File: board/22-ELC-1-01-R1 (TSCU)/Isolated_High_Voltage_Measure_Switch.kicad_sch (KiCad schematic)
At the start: 18 parts, among them U10 RFMM-0505S, U13 ACPL-C79B, U14 LM358

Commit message: Ready for review
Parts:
- renumbered C19 to C25, C35 to C26, C21 to C27, C22 to C28, C25 to C29, C26 to C30, R31 to R43, R32 to R44, R33 to R45, R34 to R46, R35 to R47, R37 to R48, R39 to R49, R38 to R50, R41 to R51, U13 to U10, U14 to U11, U10 to U9

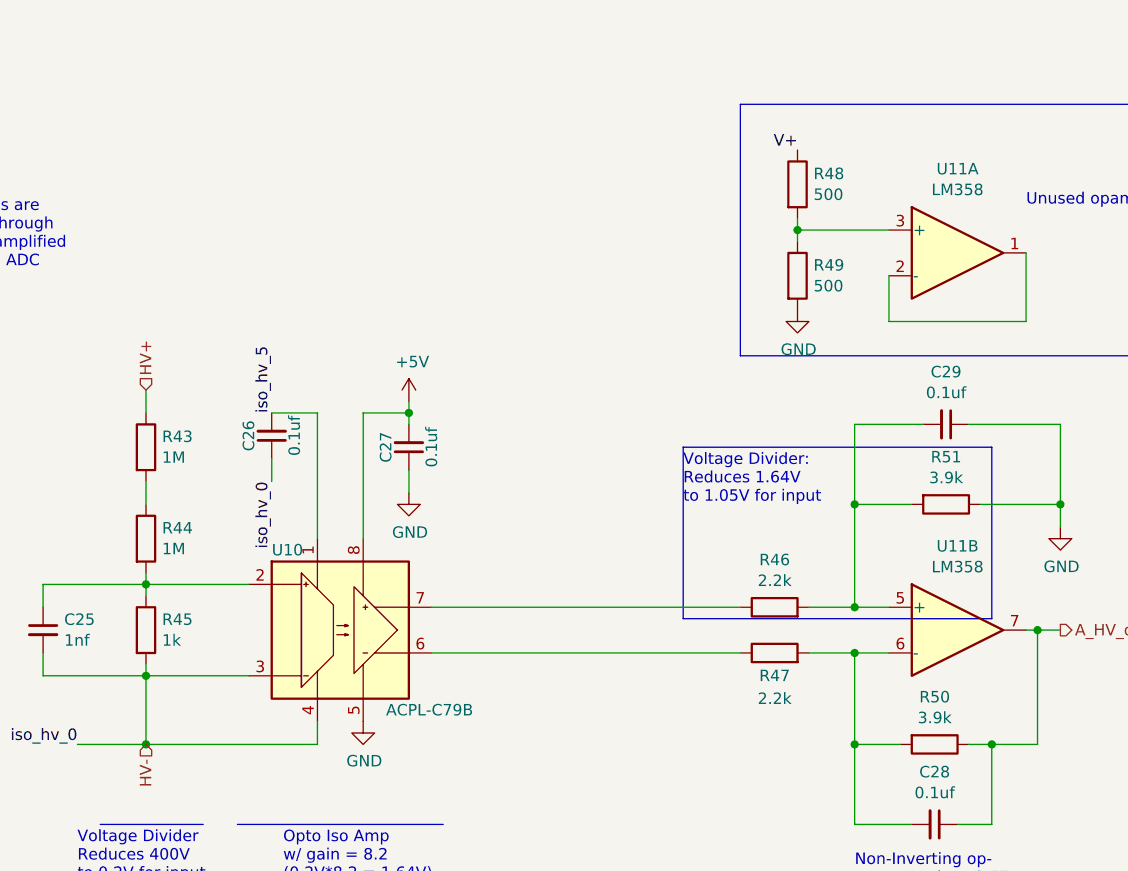
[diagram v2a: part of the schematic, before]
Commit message: All good except need to switch everything to accepting 24v power
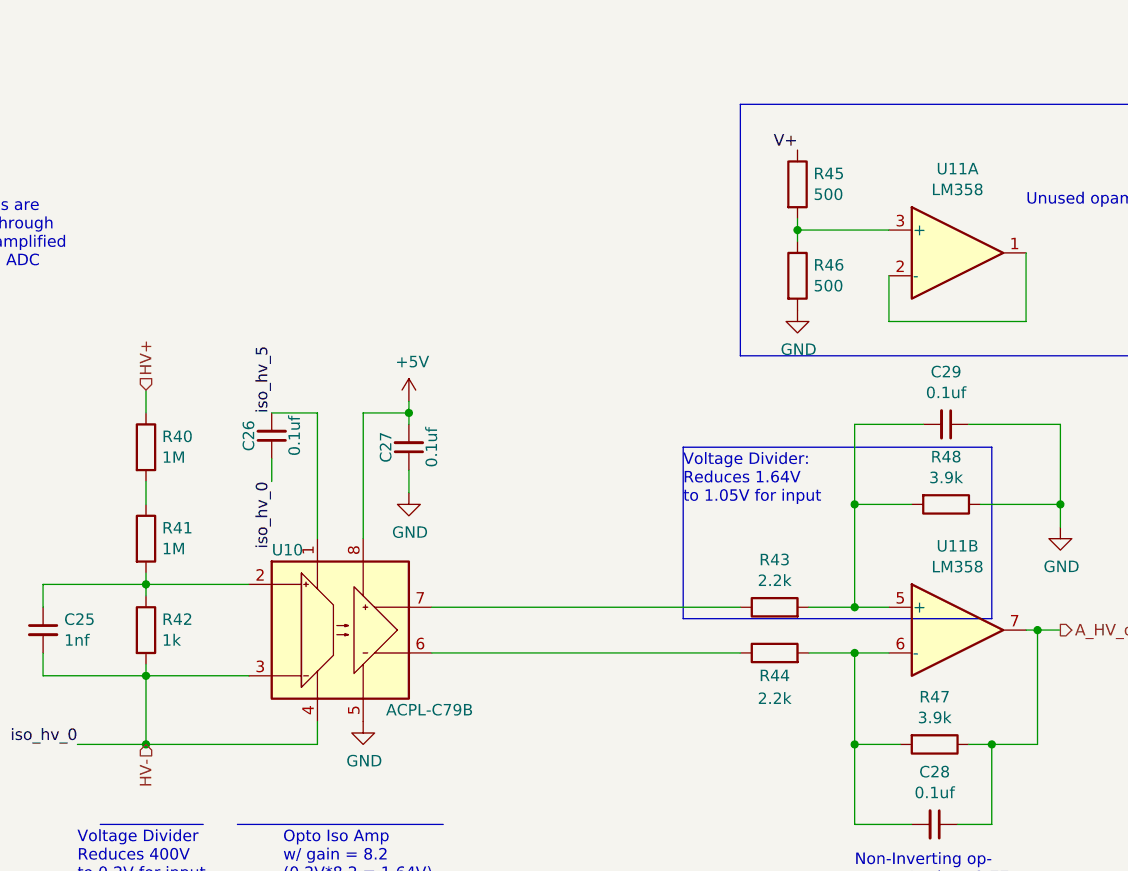
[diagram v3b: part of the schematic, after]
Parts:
- R45: renamed from R48; footprint (none) -> Resistor_SMD:R_0603_1608Metric_Pad0.98x0.95mm_HandSolder
- R46: renamed from R49; footprint (none) -> Resistor_SMD:R_0603_1608Metric_Pad0.98x0.95mm_HandSolder
- renumbered R43 to R40, R44 to R41, R45 to R42, R46 to R43, R47 to R44, R50 to R47, R51 to R48
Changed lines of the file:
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@@
   (symbol (lib_id "Device:R") (at 146.05 134.62 0) (unit 1)
     (in_bom yes) (on_board yes)
-    (property "Reference" "R45" (id 0) (at 147.828 133.4516 0)
+    (property "Reference" "R42" (id 0) (at 147.828 133.4516 0)
       (effects (font (size 1.27 1.27)) (justify left))
     )
@@
   (symbol (lib_id "Device:R") (at 146.05 124.46 0) (unit 1)
     (in_bom yes) (on_board yes)
-    (property "Reference" "R44" (id 0) (at 147.828 123.2916 0)
+    (property "Reference" "R41" (id 0) (at 147.828 123.2916 0)
       (effects (font (size 1.27 1.27)) (justify left))
     )
@@
   (symbol (lib_id "Device:R") (at 146.05 114.3 0) (unit 1)
     (in_bom yes) (on_board yes)
-    (property "Reference" "R43" (id 0) (at 147.828 113.1316 0)
+    (property "Reference" "R40" (id 0) (at 147.828 113.1316 0)
       (effects (font (size 1.27 1.27)) (justify left))
     )
@@
   (symbol (lib_id "Device:R") (at 215.9 132.08 90) (unit 1)
     (in_bom yes) (on_board yes)
-    (property "Reference" "R46" (id 0) (at 215.9 126.8222 90))
+    (property "Reference" "R43" (id 0) (at 215.9 126.8222 90))
     (property "Value" "2.2k" (id 1) (at 215.9 129.1336 90))
     (property "Footprint" "Resistor_SMD:R_0603_1608Metric_Pad0.98x0.95mm_HandSolder" (id 2) (at 215.9 133.858 90)
@@
   (symbol (lib_id "Device:R") (at 215.9 137.16 90) (unit 1)
     (in_bom yes) (on_board yes)
-    (property "Reference" "R47" (id 0) (at 215.9 139.7 90))
+    (property "Reference" "R44" (id 0) (at 215.9 139.7 90))
     (property "Value" "2.2k" (id 1) (at 215.9 142.24 90))
     (property "Footprint" "Resistor_SMD:R_0603_1608Metric_Pad0.98x0.95mm_HandSolder" (id 2) (at 215.9 138.938 90)
@@
   (symbol (lib_id "Device:R") (at 234.95 120.65 270) (unit 1)
     (in_bom yes) (on_board yes)
-    (property "Reference" "R51" (id 0) (at 234.95 115.3922 90))
+    (property "Reference" "R48" (id 0) (at 234.95 115.3922 90))
     (property "Value" "3.9k" (id 1) (at 234.95 117.7036 90))
     (property "Footprint" "Resistor_SMD:R_0603_1608Metric_Pad0.98x0.95mm_HandSolder" (id 2) (at 234.95 118.872 90)
@@
   (symbol (lib_id "Device:R") (at 233.68 147.32 270) (unit 1)
     (in_bom yes) (on_board yes)
-    (property "Reference" "R50" (id 0) (at 233.68 142.0622 90))
+    (property "Reference" "R47" (id 0) (at 233.68 142.0622 90))
     (property "Value" "3.9k" (id 1) (at 233.68 144.3736 90))
     (property "Footprint" "Resistor_SMD:R_0603_1608Metric_Pad0.98x0.95mm_HandSolder" (id 2) (at 233.68 145.542 90)
@@
   (symbol (lib_id "Device:R") (at 218.44 85.09 0) (unit 1)
     (in_bom yes) (on_board yes)
-    (property "Reference" "R48" (id 0) (at 220.218 83.9216 0)
+    (property "Reference" "R45" (id 0) (at 220.218 83.9216 0)
       (effects (font (size 1.27 1.27)) (justify left))
     )
@@
       (effects (font (size 1.27 1.27)) (justify left))
     )
-    (property "Footprint" "" (id 2) (at 216.662 85.09 90)
+    (property "Footprint" "Resistor_SMD:R_0603_1608Metric_Pad0.98x0.95mm_HandSolder" (id 2) (at 216.662 85.09 90)
       (effects (font (size 1.27 1.27)) hide)
     )
@@
   (symbol (lib_id "Device:R") (at 218.44 95.25 0) (unit 1)
     (in_bom yes) (on_board yes)
-    (property "Reference" "R49" (id 0) (at 220.218 94.0816 0)
+    (property "Reference" "R46" (id 0) (at 220.218 94.0816 0)
       (effects (font (size 1.27 1.27)) (justify left))
     )
@@
       (effects (font (size 1.27 1.27)) (justify left))
     )
-    (property "Footprint" "" (id 2) (at 216.662 95.25 90)
-      (effects (font (size 1.27 1.27)) hide)
-    )
+    (property "Footprint" "Resistor_SMD:R_0603_1608Metric_Pad0.98x0.95mm_HandSolder" (id 2) (at 216.662 95.25 90)
+      (effects (font (size 1.27 1.27)) hide)
+    )

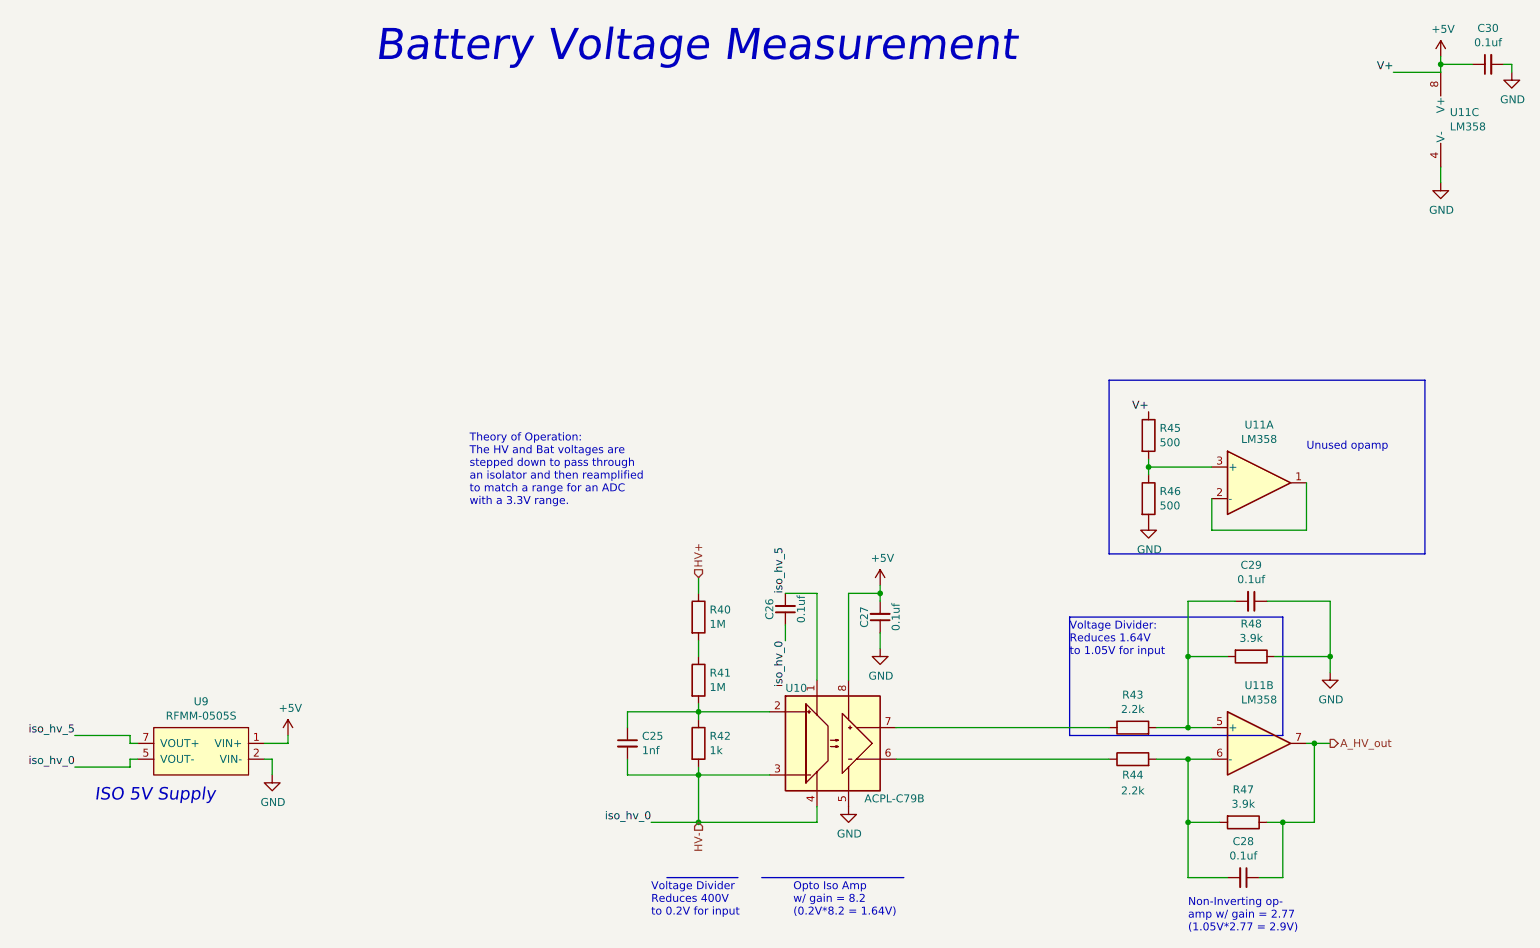
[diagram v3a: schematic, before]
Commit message: Finalized schematic, started board layout
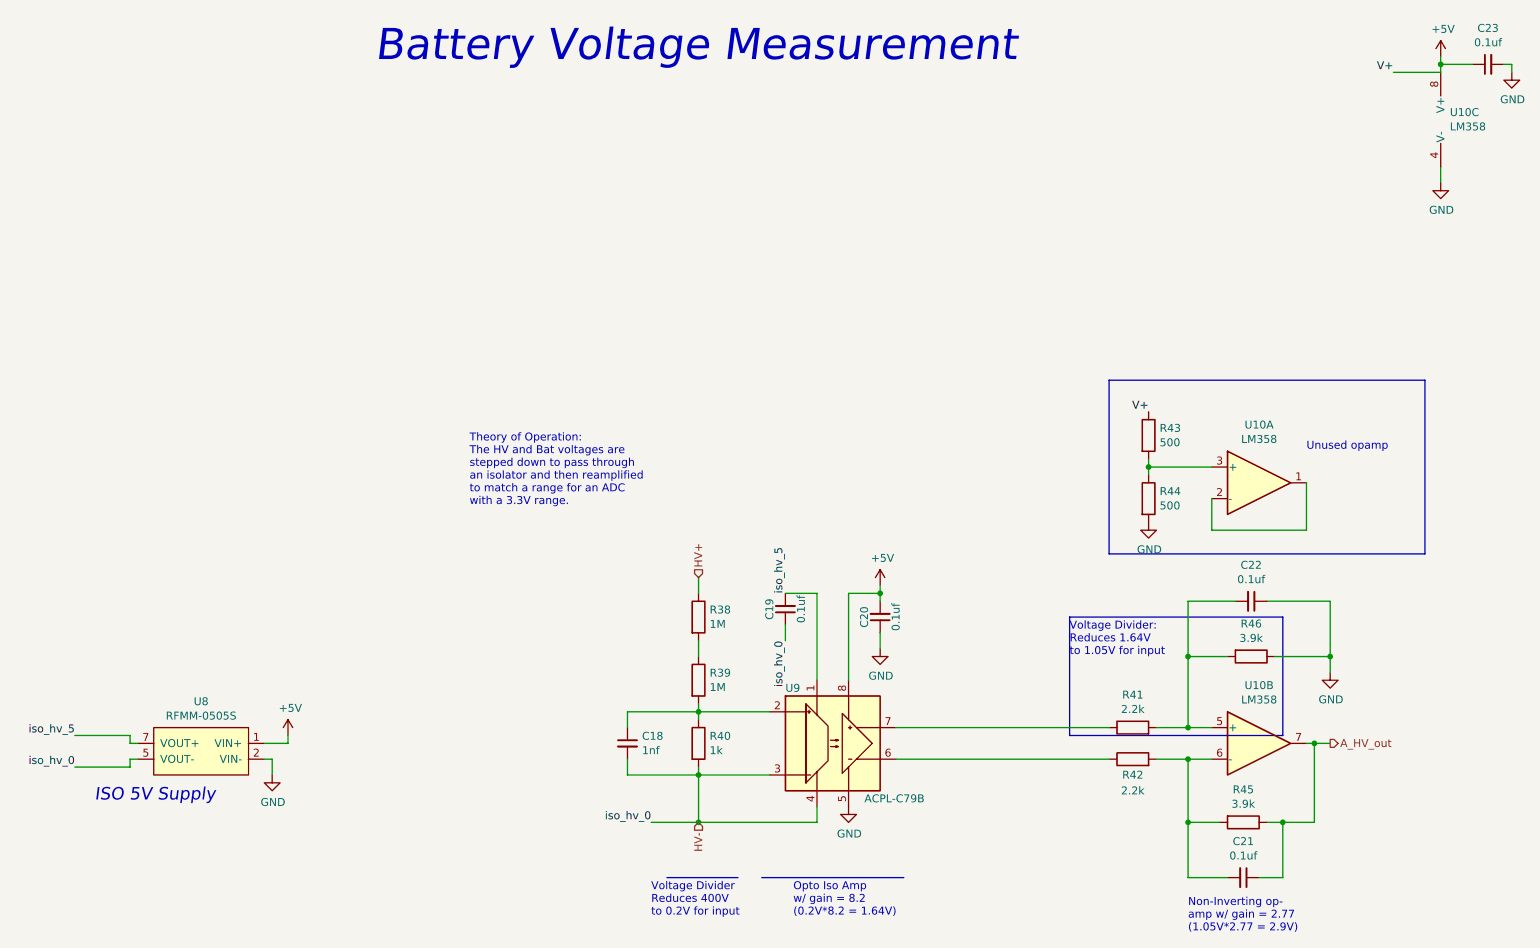
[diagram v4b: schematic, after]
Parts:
- C18: renamed from C25; footprint Capacitor_SMD:C_0603_1608Metric_Pad1.08x0.95mm_HandSolder -> Capacitor_SMD:C_0402_1005Metric
- C19: renamed from C26; footprint Capacitor_SMD:C_0603_1608Metric_Pad1.08x0.95mm_HandSolder -> Capacitor_SMD:C_0402_1005Metric
- C20: renamed from C27; footprint Capacitor_SMD:C_0603_1608Metric_Pad1.08x0.95mm_HandSolder -> Capacitor_SMD:C_0402_1005Metric
- C21: renamed from C28; footprint Capacitor_SMD:C_0603_1608Metric_Pad1.08x0.95mm_HandSolder -> Capacitor_SMD:C_0402_1005Metric
- C22: renamed from C29; footprint Capacitor_SMD:C_0603_1608Metric_Pad1.08x0.95mm_HandSolder -> Capacitor_SMD:C_0402_1005Metric
- C23: renamed from C30; footprint Capacitor_SMD:C_0603_1608Metric_Pad1.08x0.95mm_HandSolder -> Capacitor_SMD:C_0402_1005Metric
- R38: renamed from R40; footprint Resistor_SMD:R_1206_3216Metric_Pad1.30x1.75mm_HandSolder -> FixedTextSizes:R_0402_1005Metric
- R39: renamed from R41; footprint Resistor_SMD:R_1206_3216Metric_Pad1.30x1.75mm_HandSolder -> FixedTextSizes:R_0402_1005Metric
- R40: renamed from R42; footprint Resistor_SMD:R_0603_1608Metric_Pad0.98x0.95mm_HandSolder -> FixedTextSizes:R_0402_1005Metric
- R41: renamed from R43; footprint Resistor_SMD:R_0603_1608Metric_Pad0.98x0.95mm_HandSolder -> FixedTextSizes:R_0402_1005Metric
- R42: renamed from R44; footprint Resistor_SMD:R_0603_1608Metric_Pad0.98x0.95mm_HandSolder -> FixedTextSizes:R_0402_1005Metric
- R43: renamed from R45; footprint Resistor_SMD:R_0603_1608Metric_Pad0.98x0.95mm_HandSolder -> FixedTextSizes:R_0402_1005Metric
- R44: renamed from R46; footprint Resistor_SMD:R_0603_1608Metric_Pad0.98x0.95mm_HandSolder -> FixedTextSizes:R_0402_1005Metric
- R45: renamed from R47; footprint Resistor_SMD:R_0603_1608Metric_Pad0.98x0.95mm_HandSolder -> FixedTextSizes:R_0402_1005Metric
- R46: renamed from R48; footprint Resistor_SMD:R_0603_1608Metric_Pad0.98x0.95mm_HandSolder -> FixedTextSizes:R_0402_1005Metric
- renumbered U11 to U10, U9 to U8, U10 to U9

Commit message: More progress
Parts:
- C18, C19, C20, C21, C22, C23: footprint Capacitor_SMD:C_0402_1005Metric -> FixedTextSizes:C_0402_1005Metric_Pad0.74x0.62mm_HandSolder_Reasonable_Text_Size
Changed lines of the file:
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@@
   (symbol (lib_id "power:+5V") (at 80.01 133.35 0) (unit 1)
     (in_bom yes) (on_board yes)
-    (property "Reference" "#PWR082" (id 0) (at 80.01 137.16 0)
+    (property "Reference" "#PWR085" (id 0) (at 80.01 137.16 0)
       (effects (font (size 1.27 1.27)) hide)
     )
@@
   (symbol (lib_id "power:GND") (at 77.47 139.7 0) (unit 1)
     (in_bom yes) (on_board yes)
-    (property "Reference" "#PWR081" (id 0) (at 77.47 146.05 0)
+    (property "Reference" "#PWR084" (id 0) (at 77.47 146.05 0)
       (effects (font (size 1.27 1.27)) hide)
     )
@@
   (symbol (lib_id "power:GND") (at 265.43 44.45 0) (unit 1)
     (in_bom yes) (on_board yes)
-    (property "Reference" "#PWR089" (id 0) (at 265.43 50.8 0)
+    (property "Reference" "#PWR092" (id 0) (at 265.43 50.8 0)
       (effects (font (size 1.27 1.27)) hide)
     )
@@
     (property "Reference" "C23" (id 0) (at 273.05 19.5834 90))
     (property "Value" "0.1uf" (id 1) (at 273.05 21.8948 90))
-    (property "Footprint" "Capacitor_SMD:C_0402_1005Metric" (id 2) (at 273.05 25.4 0)
+    (property "Footprint" "FixedTextSizes:C_0402_1005Metric_Pad0.74x0.62mm_HandSolder_Reasonable_Text_Size" (id 2) (at 273.05 25.4 0)
       (effects (font (size 1.27 1.27)) hide)
     )
@@
   (symbol (lib_id "power:GND") (at 276.86 26.67 0) (unit 1)
     (in_bom yes) (on_board yes)
-    (property "Reference" "#PWR090" (id 0) (at 276.86 33.02 0)
+    (property "Reference" "#PWR093" (id 0) (at 276.86 33.02 0)
       (effects (font (size 1.27 1.27)) hide)
     )
@@
   (symbol (lib_id "power:GND") (at 170.18 144.78 0) (unit 1)
     (in_bom yes) (on_board yes)
-    (property "Reference" "#PWR083" (id 0) (at 170.18 151.13 0)
+    (property "Reference" "#PWR086" (id 0) (at 170.18 151.13 0)
       (effects (font (size 1.27 1.27)) hide)
     )
@@
   (symbol (lib_id "power:GND") (at 175.26 119.38 0) (unit 1)
     (in_bom yes) (on_board yes)
-    (property "Reference" "#PWR085" (id 0) (at 175.26 125.73 0)
+    (property "Reference" "#PWR088" (id 0) (at 175.26 125.73 0)
       (effects (font (size 1.27 1.27)) hide)
     )
@@
       (effects (font (size 1.27 1.27)) (justify left))
     )
-    (property "Footprint" "Capacitor_SMD:C_0402_1005Metric" (id 2) (at 134.62 134.62 0)
+    (property "Footprint" "FixedTextSizes:C_0402_1005Metric_Pad0.74x0.62mm_HandSolder_Reasonable_Text_Size" (id 2) (at 134.62 134.62 0)
       (effects (font (size 1.27 1.27)) hide)
     )
@@
     (property "Reference" "C20" (id 0) (at 172.72 114.3 90))
     (property "Value" "0.1uf" (id 1) (at 177.8 114.3 90))
-    (property "Footprint" "Capacitor_SMD:C_0402_1005Metric" (id 2) (at 175.26 114.3 0)
+    (property "Footprint" "FixedTextSizes:C_0402_1005Metric_Pad0.74x0.62mm_HandSolder_Reasonable_Text_Size" (id 2) (at 175.26 114.3 0)
       (effects (font (size 1.27 1.27)) hide)
     )
@@
     (property "Reference" "C21" (id 0) (at 233.68 150.3934 90))
     (property "Value" "0.1uf" (id 1) (at 233.68 152.7048 90))
-    (property "Footprint" "Capacitor_SMD:C_0402_1005Metric" (id 2) (at 233.68 156.21 0)
+    (property "Footprint" "FixedTextSizes:C_0402_1005Metric_Pad0.74x0.62mm_HandSolder_Reasonable_Text_Size" (id 2) (at 233.68 156.21 0)
       (effects (font (size 1.27 1.27)) hide)
     )
@@
     (property "Reference" "C22" (id 0) (at 234.95 105.9434 90))
     (property "Value" "0.1uf" (id 1) (at 234.95 108.2548 90))
-    (property "Footprint" "Capacitor_SMD:C_0402_1005Metric" (id 2) (at 234.95 111.76 0)
+    (property "Footprint" "FixedTextSizes:C_0402_1005Metric_Pad0.74x0.62mm_HandSolder_Reasonable_Text_Size" (id 2) (at 234.95 111.76 0)
       (effects (font (size 1.27 1.27)) hide)
     )
@@
   (symbol (lib_id "power:GND") (at 247.65 123.19 0) (unit 1)
     (in_bom yes) (on_board yes)
-    (property "Reference" "#PWR087" (id 0) (at 247.65 129.54 0)
+    (property "Reference" "#PWR090" (id 0) (at 247.65 129.54 0)
       (effects (font (size 1.27 1.27)) hide)
     )
@@
   (symbol (lib_id "power:+5V") (at 175.26 109.22 0) (unit 1)
     (in_bom yes) (on_board yes)
-    (property "Reference" "#PWR084" (id 0) (at 175.26 113.03 0)
+    (property "Reference" "#PWR087" (id 0) (at 175.26 113.03 0)
       (effects (font (size 1.27 1.27)) hide)
     )
@@
   (symbol (lib_id "power:+5V") (at 265.43 24.13 0) (unit 1)
     (in_bom yes) (on_board yes)
-    (property "Reference" "#PWR088" (id 0) (at 265.43 27.94 0)
+    (property "Reference" "#PWR091" (id 0) (at 265.43 27.94 0)
       (effects (font (size 1.27 1.27)) hide)
     )
@@
     (property "Reference" "C19" (id 0) (at 157.48 113.03 90))
     (property "Value" "0.1uf" (id 1) (at 162.56 113.03 90))
-    (property "Footprint" "Capacitor_SMD:C_0402_1005Metric" (id 2) (at 160.02 113.03 0)
+    (property "Footprint" "FixedTextSizes:C_0402_1005Metric_Pad0.74x0.62mm_HandSolder_Reasonable_Text_Size" (id 2) (at 160.02 113.03 0)
       (effects (font (size 1.27 1.27)) hide)
     )
@@
   (symbol (lib_id "power:GND") (at 218.44 99.06 0) (unit 1)
     (in_bom yes) (on_board yes)
-    (property "Reference" "#PWR086" (id 0) (at 218.44 105.41 0)
-      (effects (font (size 1.27 1.27)) hide)
-    )
+    (property "Reference" "#PWR089" (id 0) (at 218.44 105.41 0)
+      (effects (font (size 1.27 1.27)) hide)
+    )
